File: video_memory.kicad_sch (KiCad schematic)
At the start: 22 parts, among them J11 74LS245, J9 uPD446, K15 74LS04, U2 74LS10

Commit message: Removed some dangling notes
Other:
- note added: "Attribute RAM"
- note removed: "Bus is shared with video memory H9"
- note removed: "WE and OE are same as H9"
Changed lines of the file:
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@@
     (stroke (width 0) (type default))
   )
-  (text "WE and OE\nare same as H9" (at 190.5 82.55 0)
+  (text "Attribute\n   RAM" (at 163.83 109.22 0)
     (effects (font (size 1.27 1.27)) (justify left bottom))
   )
@@
     (effects (font (size 1.27 1.27)) (justify left bottom))
   )
-  (text "Bus is shared with video memory H9" (at 201.93 86.36 0)
-    (effects (font (size 1.27 1.27)) (justify left bottom))
-  )

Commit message: video gen and memory: wire renaming, but something is still missing
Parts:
- added K15: 7417, symbol 74xx:74LS04
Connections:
- net vmem0: now also J9.8 (A0)
- net vmem1: now also J9.7 (A1)
- net vmem10: now also J9.19 (A10)
- net vmem2: now also J9.6 (A2)
- net vmem3: now also J9.5 (A3)
- net vmem4: now also J9.4 (A4)
- net vmem5: now also J9.3 (A5)
- net vmem6: now also J9.2 (A6)
- net vmem7: now also J9.1 (A7)
- net vmem8: now also J9.23 (A8)
- net vmem9: now also J9.22 (A9)
- net attrmd7: now reaches J11.11 (B7)
- net attrmd7: now also J9.17 (D7)
- net attrmd6: now reaches J11.12 (B6)
- net attrmd6: now also J9.16 (D6)
- net attrmd5: now reaches J11.13 (B5)
- net attrmd5: now also J9.15 (D5)
- net attrmd4: now reaches J11.14 (B4)
- net attrmd4: now also J9.14 (D4)
- net attrmd3: now reaches J11.15 (B3)
- net attrmd3: now also J9.13 (D3)
- net attrmd2: now reaches J11.16 (B2)
- net attrmd2: now also J9.11 (D2)
- net attrmd1: now reaches J11.17 (B1)
- net attrmd1: now also J9.10 (D1)
- net attrmd0: now reaches J11.18 (B0)
- net attrmd0: now also J9.9 (D0)
- net chmd0: now reaches J11.2 (A0)
- net chmd0: now also F11.18 (Y0), F12.3 (D0), H8H10.9 (D0)
- net chmd1: now reaches J11.3 (A1)
- net chmd1: now also F11.17 (Y1), F12.4 (D1), H8H10.10 (D1)
- net chmd2: now reaches J11.4 (A2)
- net chmd2: now also F11.16 (Y2), F12.7 (D2), H8H10.11 (D2)
- net chmd3: now reaches J11.5 (A3)
- net chmd3: now also F11.15 (Y3), F12.8 (D3), H8H10.13 (D3)
- net chmd4: now reaches J11.6 (A4)
- net chmd4: now also F11.14 (Y4), F12.13 (D4), H8H10.14 (D4)
- net chmd5: now reaches J11.7 (A5)
- net chmd5: now also F11.13 (Y5), F12.14 (D5), H8H10.15 (D5)
- net chmd6: now reaches J11.8 (A6)
- net chmd6: now also F11.12 (Y6), F12.17 (D6), H8H10.16 (D6)
- net chmd7: now reaches J11.9 (A7)
- net chmd7: now also F11.11 (Y7), F12.18 (D7), H8H10.17 (D7)
- net A7: now reaches F9.10 (I1c)
- net A6: now reaches F9.13 (I1d)
- net A4: now reaches F9.3 (I1a)
- net A5: now reaches F9.6 (I1b)
- net d0: now reaches F11.2 (A0)
- net d0: now also F12.2 (O0)
- net d1: now reaches F11.3 (A1)
- net d1: now also F12.5 (O1)
- net d2: now reaches F11.4 (A2)
- net d2: now also F12.6 (O2)
- net d3: now reaches F11.5 (A3)
- net d3: now also F12.9 (O3)
- net d4: now reaches F11.6 (A4)
- net d4: now also F12.12 (O4)
- net d5: now reaches F11.7 (A5)
- net d5: now also F12.15 (O5)
- net d6: now reaches F11.8 (A6)
- net d6: now also F12.16 (O6)
- net d7: now reaches F11.9 (A7)
- net d7: now also F12.19 (O7)
- net A10: now reaches F10.10 (I1c)
- net A8: now reaches F10.3 (I1a)
- net A9: now reaches F10.6 (I1b)
- net A3: now reaches F8.10 (I1c)
- net A2: now reaches F8.13 (I1d)
- net A0: now reaches F8.3 (I1a)
- net A1: now reaches F8.6 (I1b)
- net at E14.6 (~{Q}): now also K15.9
- net MainClock renamed CRTC_CLK
- net ma0 renamed VMA0
- net ma1 renamed VMA1
- net ma10 renamed VMA10
- net ma2 renamed VMA2
- net ma3 renamed VMA3
- net ma4 renamed VMA4
- net ma5 renamed VMA5
- net ma6 renamed VMA6
- net ma7 renamed VMA7
- net ma8 renamed VMA8
- net ma9 renamed VMA9
- net vmem_karmic renamed z80_vmem_sample
- net vmem_oniric renamed ~{z80_vmem_req}
- net ~{RD|WR}: no longer names the net of H1.1, L3.8
- new net ~{WAIT}: K15.8
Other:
- note added: "z80_char_enable"
- note added: "~{RD|WR}. Why not ~{IOREQ}? Nice question..."
- note removed: "TODO"
- moved on the sheet: E14A, E14B, E15B, F14C, H1A, J11, K15D, L3C

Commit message: Fixed typo in video generation. Added some useful (I hope) notes.
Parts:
- removed K15: 74LS04, symbol 74xx:74LS04
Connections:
- net MUXSEL renamed ~{CRTC_CLK}
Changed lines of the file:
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@@
-    (stroke (width 0) (type default))
-  )
-  (wire (pts (xy 45.72 264.16) (xy 55.88 264.16))
     (stroke (width 0) (type default))
   )
@@
     (stroke (width 0) (type default))
   )
-  (wire (pts (xy 86.36 255.27) (xy 76.2 255.27))
-    (stroke (width 0) (type default))
-  )
-  (wire (pts (xy 27.94 264.16) (xy 30.48 264.16))
+  (wire (pts (xy 59.69 255.27) (xy 86.36 255.27))
     (stroke (width 0) (type default))
   )
@@
     (effects (font (size 1.27 1.27)) (justify left bottom))
   )
-  (label "MUXSEL" (at 55.88 264.16 180) (fields_autoplaced)
-    (effects (font (size 1.27 1.27)) (justify right bottom))
-  )
   (label "d7" (at 322.58 110.49 0) (fields_autoplaced)
     (effects (font (size 1.27 1.27)) (justify left bottom))
@@
     (effects (font (size 1.27 1.27)) (justify right bottom))
   )
-  (label "MUXSEL" (at 76.2 255.27 0) (fields_autoplaced)
+  (label "MUXSEL" (at 67.31 255.27 0) (fields_autoplaced)
     (effects (font (size 1.27 1.27)) (justify left bottom))
   )
@@
     )
   )
-  (global_label "CRTC_CLK" (shape input) (at 27.94 264.16 180) (fields_autoplaced)
+  (global_label "~{CRTC_CLK}" (shape input) (at 59.69 255.27 180) (fields_autoplaced)
     (effects (font (size 1.27 1.27)) (justify right))
-    (property "Intersheetrefs" "${INTERSHEET_REFS}" (at 15.6415 264.16 0)
+    (property "Intersheetrefs" "${INTERSHEET_REFS}" (at 47.3915 255.27 0)
       (effects (font (size 1.27 1.27)) (justify right) hide)
     )
@@
         )
       )
-    )
-  )
-  (symbol (lib_id "74xx:74LS04") (at 38.1 264.16 0) (unit 4)
-    (in_bom yes) (on_board yes) (dnp no) (fields_autoplaced)
-    (property "Reference" "K15" (at 38.1 255.27 0)
-      (effects (font (size 1.27 1.27)))
-    )
-    (property "Value" "74LS04" (at 38.1 257.81 0)
-      (effects (font (size 1.27 1.27)))
-    )
-    (property "Footprint" "" (at 38.1 264.16 0)
-      (effects (font (size 1.27 1.27)) hide)
-    )
-    (property "Datasheet" "http://www.ti.com/lit/gpn/sn74LS04" (at 38.1 264.16 0)
-      (effects (font (size 1.27 1.27)) hide)
-    )
-    (pin "1")
-    (pin "2")
-    (pin "3")
-    (pin "4")
-    (pin "5")
-    (pin "6")
-    (pin "8")
-    (pin "9")
-    (pin "10")
-    (pin "11")
-    (pin "12")
-    (pin "13")
-    (pin "14")
-    (pin "7")
-    (instances
-      (project "ceda"
-        (path "/12a6dbe3-008d-4c5b-88f6-9f1c816060be/23c42ab9-740a-4e84-88f1-9f74965e7273"
-          (reference "K15") (unit 4)
-        )
-        (path "/12a6dbe3-008d-4c5b-88f6-9f1c816060be/3df68a1a-abd3-4ad7-9eb9-855dfc37a3a7"
-          (reference "K15") (unit 4)
-        )
-      )

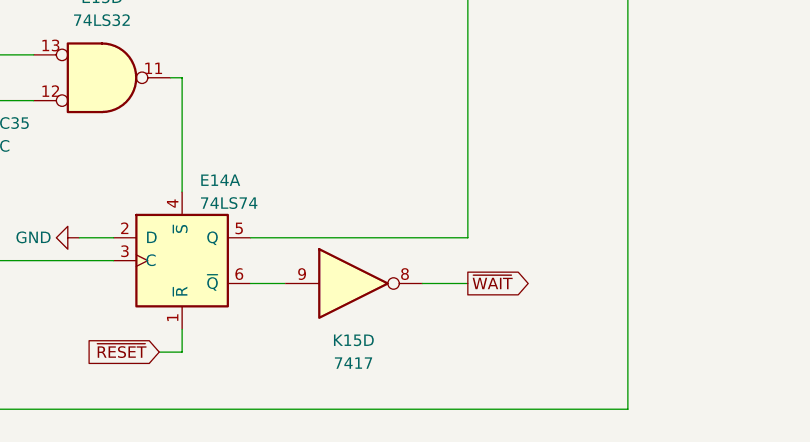
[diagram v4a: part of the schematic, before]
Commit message: Graphical error: 7417 is a non-inverting buffer
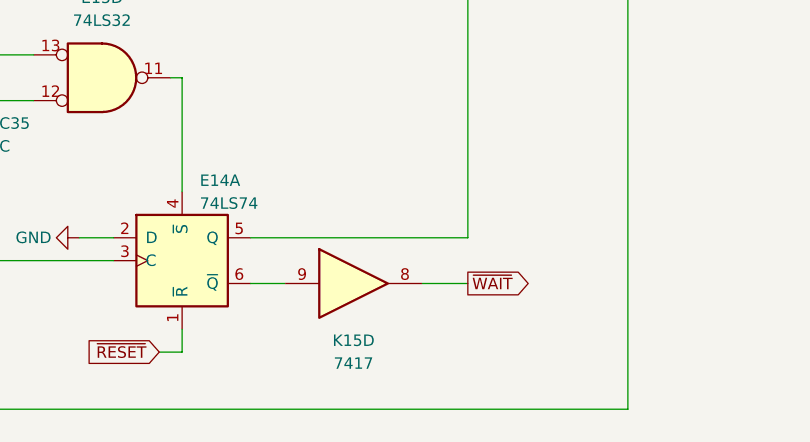
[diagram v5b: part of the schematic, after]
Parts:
- K15: symbol 74xx:74LS04 -> 74xx:74LS07
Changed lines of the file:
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@@
     )
   )
-  (symbol (lib_id "74xx:74LS04") (at 161.29 260.35 0) (unit 4)
+  (symbol (lib_id "74xx:74LS07") (at 161.29 260.35 0) (unit 4)
     (in_bom yes) (on_board yes) (dnp no) (fields_autoplaced)
     (property "Reference" "K15" (at 161.29 266.7 0)
@@
         )
         (path "/12a6dbe3-008d-4c5b-88f6-9f1c816060be/3df68a1a-abd3-4ad7-9eb9-855dfc37a3a7"
-          (reference "KUC2") (unit 4)
+          (reference "UC2") (unit 4)
         )
       )

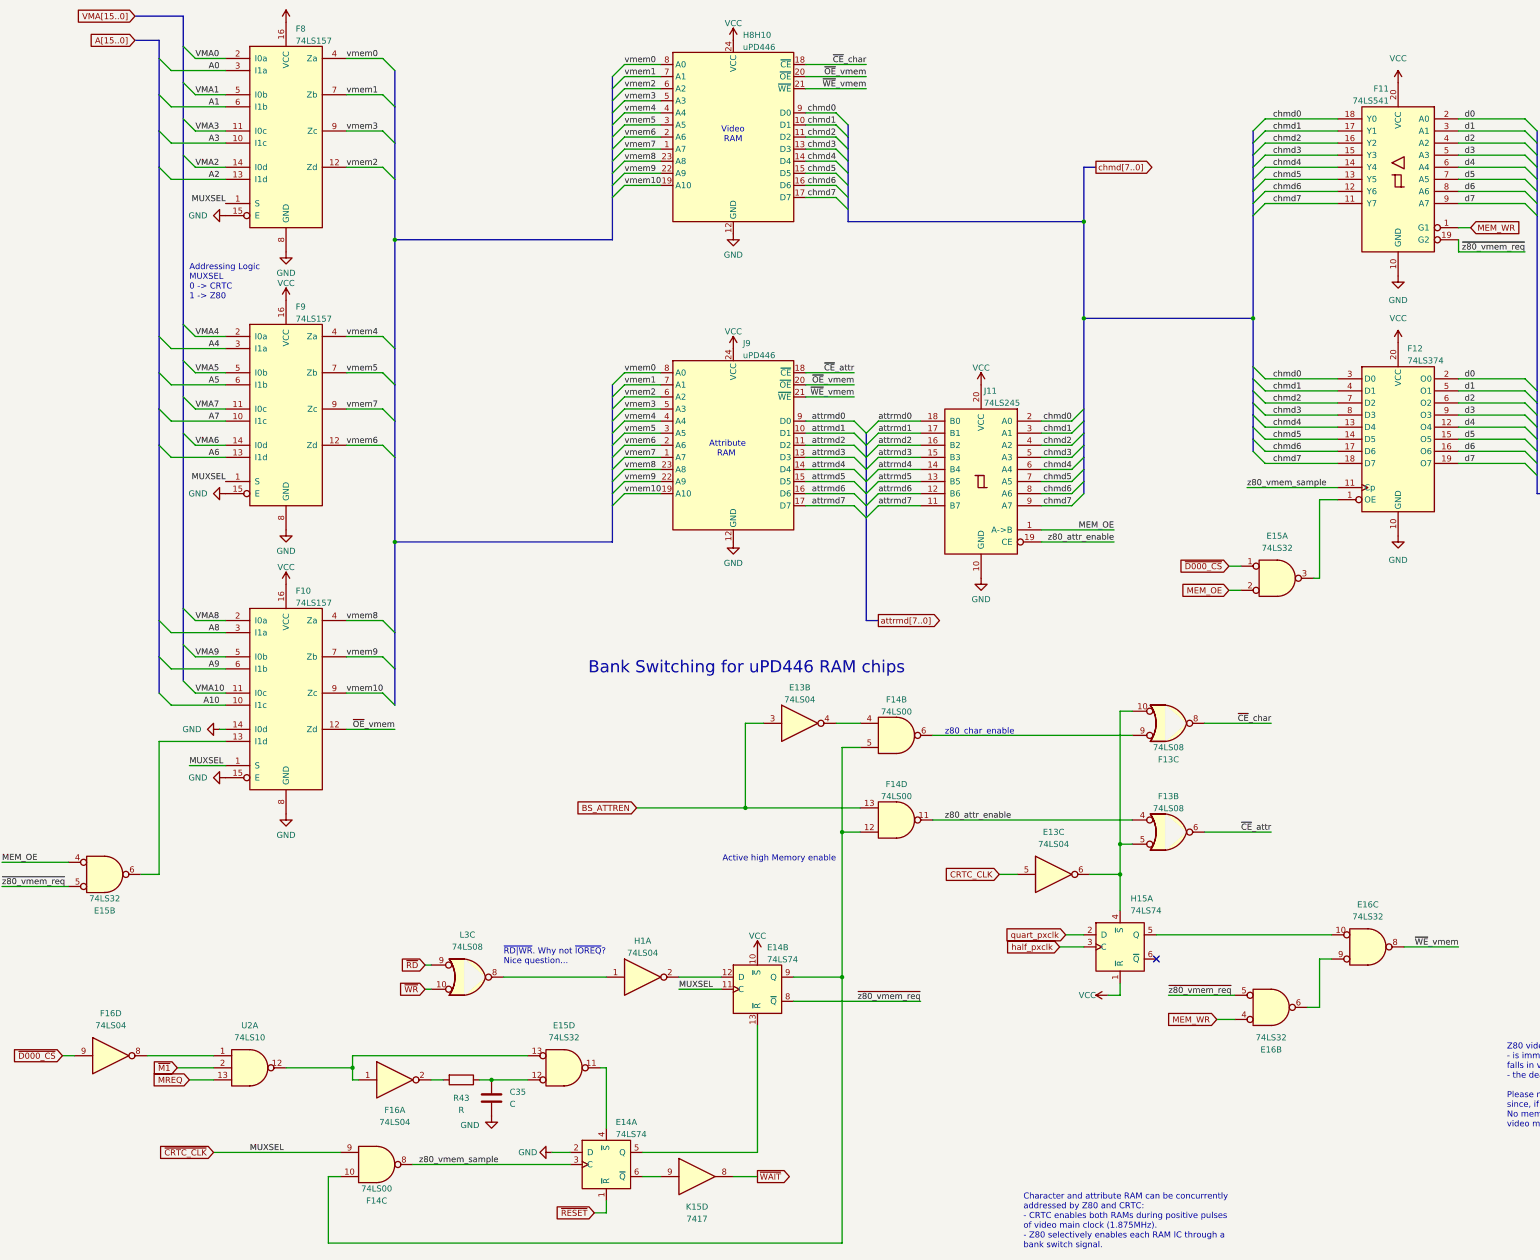
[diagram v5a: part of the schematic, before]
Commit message: Components renaming according to the Uxy convention.
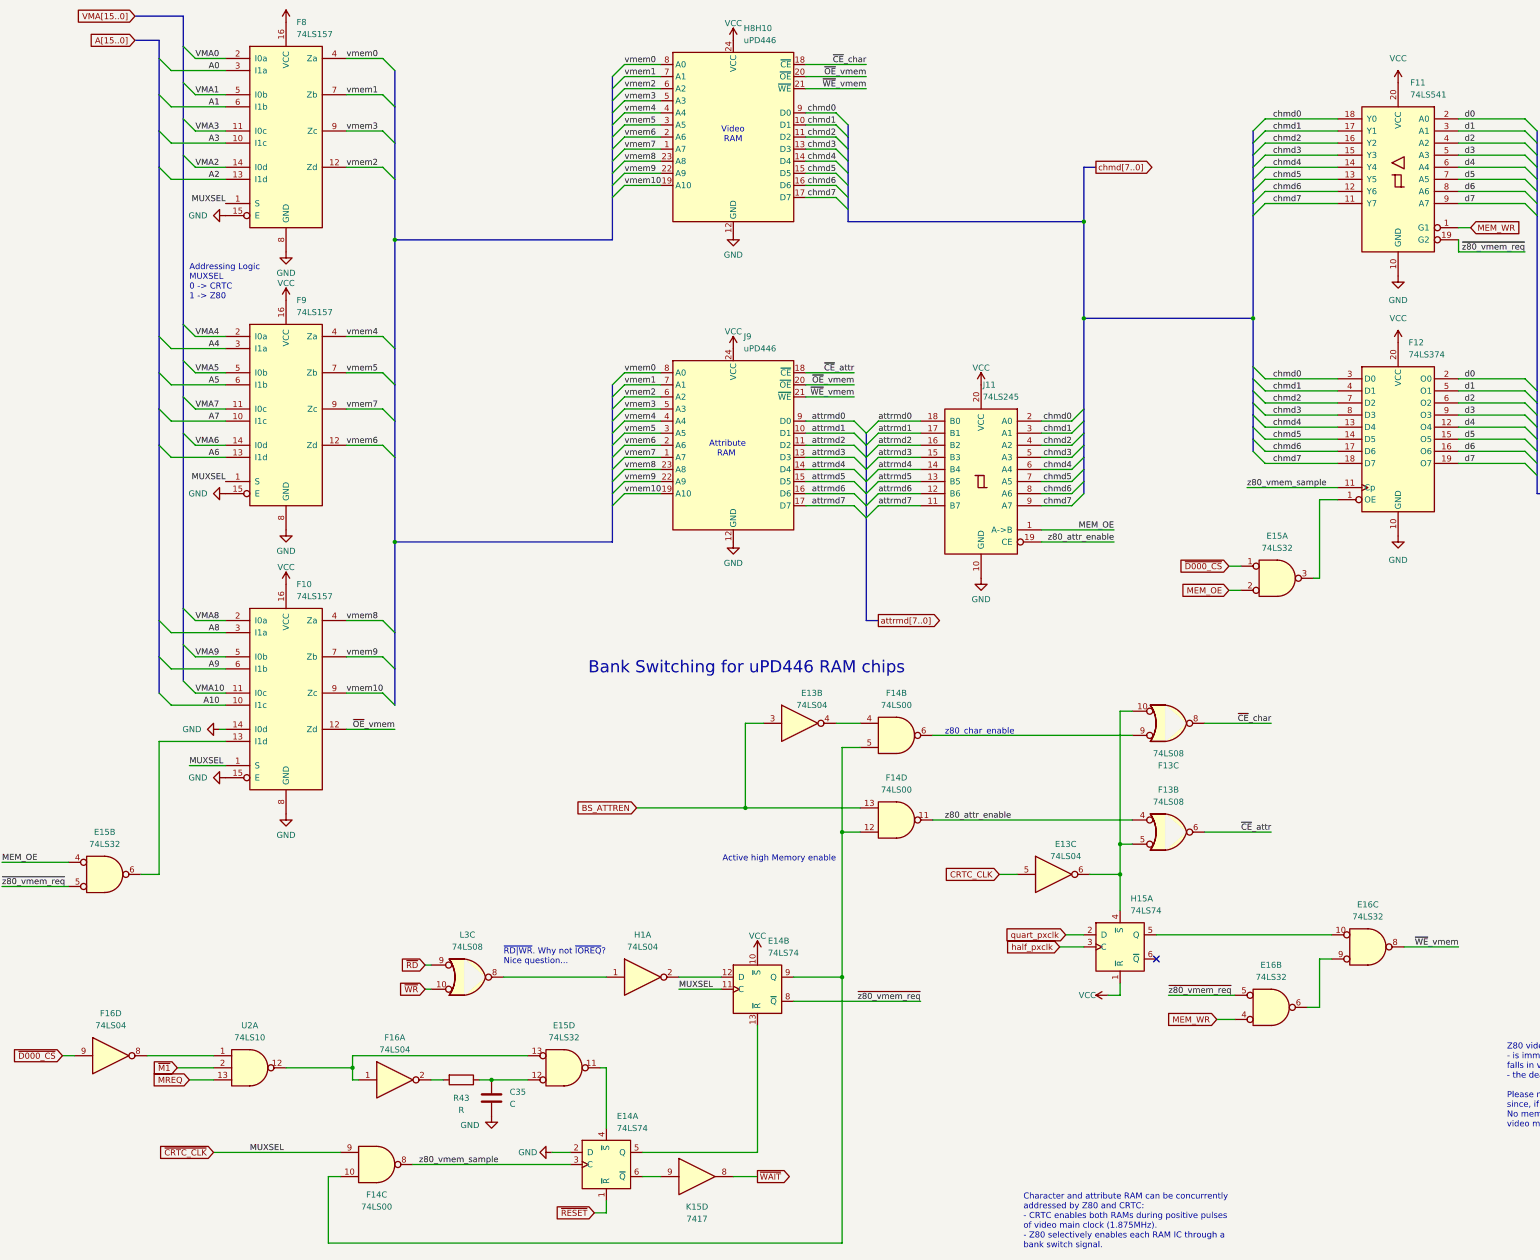
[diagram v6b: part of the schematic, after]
